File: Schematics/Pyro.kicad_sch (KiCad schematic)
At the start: 6 parts, among them J4 Drouge, Q2 IRLML2502TRPBF

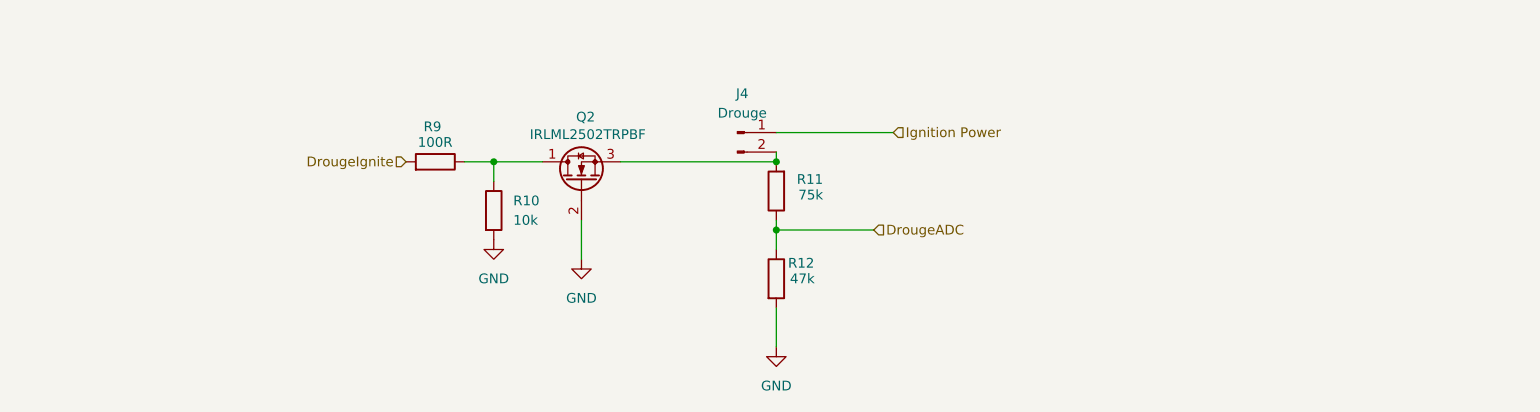
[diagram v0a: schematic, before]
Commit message: added aux pyro added reverse polarity protection re routed just need to clean up and check pin assignments
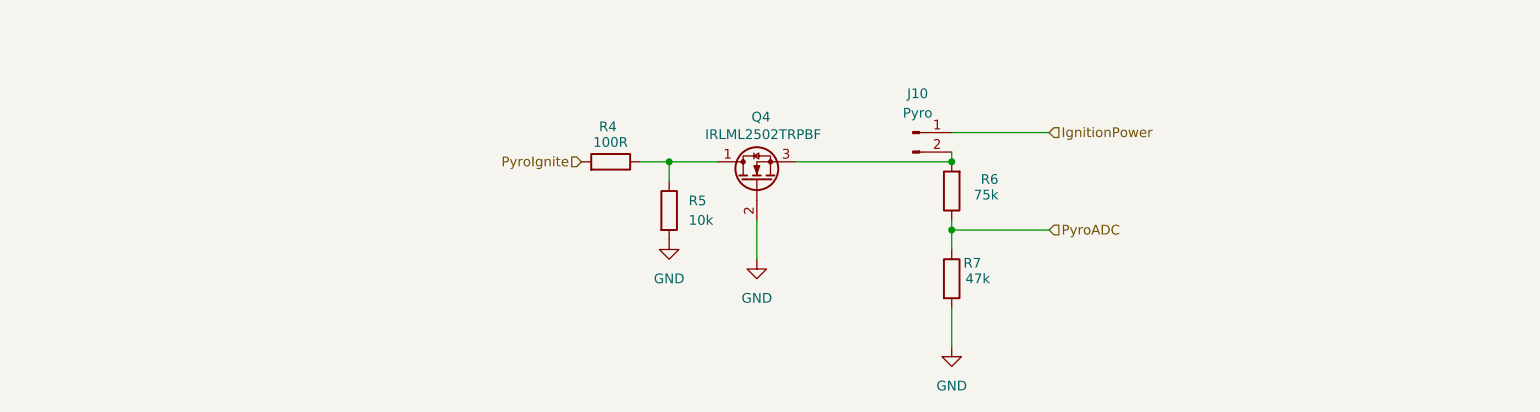
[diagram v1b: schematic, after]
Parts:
- removed J4: Drouge, myFootprints:MOLEX_26013114, symbol Connector:Conn_01x02_Pin
- removed Q2: IRLML2502TRPBF, myFootprints:SOT23, symbol Transistor_FET:Q_NMOS_DGS
- removed R10: 10k, Resistor_SMD:R_0805_2012Metric_Pad1.20x1.40mm_HandSolder, symbol Device:R
- removed R11: 75k, Resistor_SMD:R_0805_2012Metric_Pad1.20x1.40mm_HandSolder, symbol Device:R
- removed R12: 47k, Resistor_SMD:R_0805_2012Metric_Pad1.20x1.40mm_HandSolder, symbol Device:R
- removed R9: 100R, Resistor_SMD:R_0805_2012Metric_Pad1.20x1.40mm_HandSolder, symbol Device:R
- added J10: Pyro, myFootprints:MOLEX_26013114, symbol Connector:Conn_01x02_Pin
- added Q4: IRLML2502TRPBF, myFootprints:SOT23, symbol Transistor_FET:Q_NMOS_DGS
- added R4: 100R, Resistor_SMD:R_0805_2012Metric_Pad1.20x1.40mm_HandSolder, symbol Device:R
- added R5: 10k, Resistor_SMD:R_0805_2012Metric_Pad1.20x1.40mm_HandSolder, symbol Device:R
- added R6: 75k, Resistor_SMD:R_0805_2012Metric_Pad1.20x1.40mm_HandSolder, symbol Device:R
- added R7: 47k, Resistor_SMD:R_0805_2012Metric_Pad1.20x1.40mm_HandSolder, symbol Device:R
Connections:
- net GND: now also Q4.2 (G), R5.2, R7.2
- new net: J10.2 (Pin_2), Q4.3 (S), R6.2
- new net: Q4.1 (D), R4.1, R5.1
- new net IgnitionPower: J10.1 (Pin_1)
- new net PyroADC: R6.1, R7.1
- new net PyroIgnite: R4.2

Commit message: layout completed added testpoints and verified mosfet ect
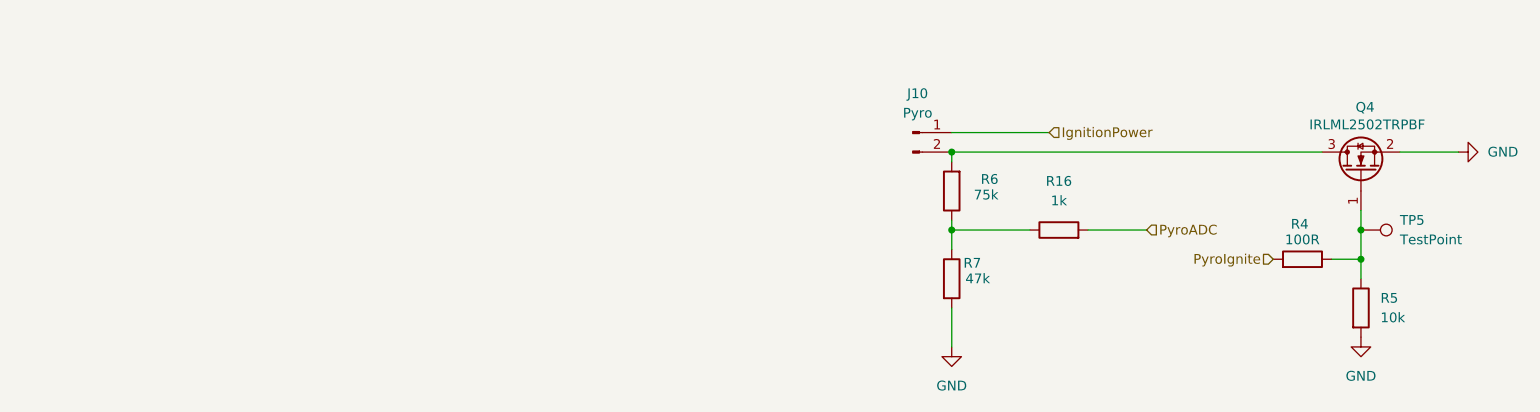
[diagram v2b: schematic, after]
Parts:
- added R16: 1k, Resistor_SMD:R_0805_2012Metric_Pad1.20x1.40mm_HandSolder, symbol Device:R
- added TP5: TestPoint, TestPoint:TestPoint_Pad_1.5x1.5mm, symbol Connector:TestPoint
- Q4: symbol Transistor_FET:Q_NMOS_DGS -> Transistor_FET:Q_NMOS_GSD
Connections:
- net PyroADC: now also R16.2; no longer R6.1, R7.1
- net at Q4.1 (G), R4.1, R5.1: now also TP5.1
- new net: R16.1, R6.1, R7.1
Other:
- moved on the sheet: Q4, R4, R5

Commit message: added comments, awaiting review
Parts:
- R16: LCSC (none) -> C95781
- TP5: now left out of the parts list
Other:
- note added: "Continuity detection with adc resistors to protect adc pins"
- note added: "Low-Side Mosfet Switch for pulling igniton to ground"
- moved on the sheet: J10, Q4, R16, R4, R5, R6, R7, TP5

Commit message: updated to KiCad 10.0, updated .gitignore
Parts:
- J10: now left out of the parts list
- R16: LCSC C95781 -> C17513
- R5: LCSC C84376 -> C17414
- R7: LCSC C2933415 -> C17713
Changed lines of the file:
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@@
 			)
 		)
-		(property "LCSC" "C84376"
+		(property "LCSC" "C17414"
 			(at 157.48 95.25 0)
 			(effects
@@
 			)
 		)
-		(property "LCSC" "C2933415"
+		(property "LCSC" "C17713"
 			(at 104.14 91.44 0)
 			(effects
@@
 			)
 		)
-		(property "LCSC" "C95781"
+		(property "LCSC" "C17513"
 			(at 118.11 85.09 90)
 			(effects
@@
 		(unit 1)
 		(exclude_from_sim no)
-		(in_bom yes)
+		(in_bom no)
 		(on_board yes)
 		(dnp no)
